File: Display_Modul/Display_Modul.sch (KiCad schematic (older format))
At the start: 14 parts, among them J101 Conn_01x08_Male, J102 Conn_02x08_Counter_Clockwise, SW101 Rotary_Encoder_Switch

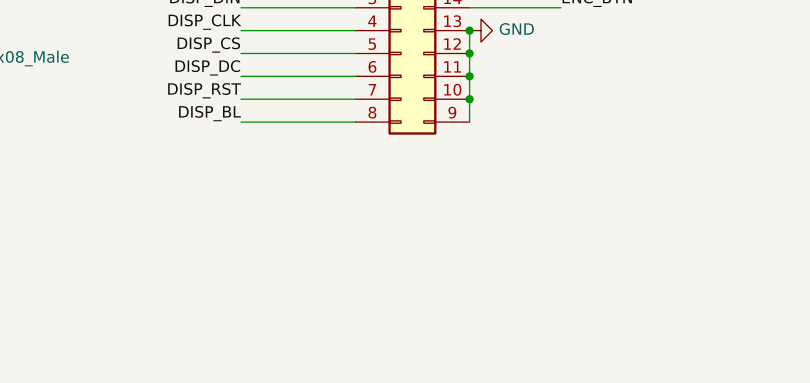
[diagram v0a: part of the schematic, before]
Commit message: Feeder Rails hinzugefügt
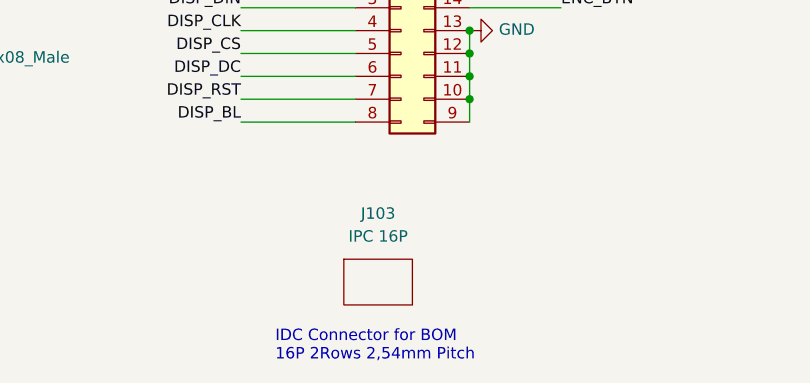
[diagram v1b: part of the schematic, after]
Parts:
- added J103: IPC 16P, ProjectFootprints:Empty, symbol PorjectLibrary:Empty
- H101, H102, H103, H104, J101: LCSC (none) -> 0
- J102: LCSC (none) -> C3406
- SW101: LCSC (none) -> C1322538
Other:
- note added: "IDC Connector for BOM\n16P 2Rows 2,54mm Pitch"
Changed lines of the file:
@@
 F 2 "Rotary_Encoder:RotaryEncoder_Alps_EC11E-Switch_Vertical_H20mm_CircularMountingHoles" H 5300 3310 50  0001 C CNN
 F 3 "~" H 5450 3410 50  0001 C CNN
+F 4 "C1322538" H 5450 3150 50  0001 C CNN "LCSC"
 	1    5450 3150
 	1    0    0    -1
@@
 F 2 "ProjectFootprints:ST7789_Waveshare" H 3850 4650 50  0001 C CNN
 F 3 "~" H 3850 4650 50  0001 C CNN
+F 4 "0" H 3850 4650 50  0001 C CNN "LCSC"
 	1    3850 4650
 	-1   0    0    -1
@@
 F 2 "ProjectFootprints:DisplayConnector" H 5950 4650 50  0001 C CNN
 F 3 "~" H 5950 4650 50  0001 C CNN
+F 4 "C3406" H 5950 4650 50  0001 C CNN "LCSC"
 	1    5950 4650
 	1    0    0    -1
@@
 F 2 "MountingHole:MountingHole_3.2mm_M3_Pad_Via" H 8000 3000 50  0001 C CNN
 F 3 "~" H 8000 3000 50  0001 C CNN
+F 4 "0" H 8000 3000 50  0001 C CNN "LCSC"
 	1    8000 3000
 	0    1    1    0
@@
 F 2 "MountingHole:MountingHole_3.2mm_M3_Pad_Via" H 8000 3200 50  0001 C CNN
 F 3 "~" H 8000 3200 50  0001 C CNN
+F 4 "0" H 8000 3200 50  0001 C CNN "LCSC"
 	1    8000 3200
 	0    1    1    0
@@
 F 2 "MountingHole:MountingHole_3.2mm_M3_Pad_Via" H 8000 3400 50  0001 C CNN
 F 3 "~" H 8000 3400 50  0001 C CNN
+F 4 "0" H 8000 3400 50  0001 C CNN "LCSC"
 	1    8000 3400
 	0    1    1    0
@@
 F 2 "MountingHole:MountingHole_3.2mm_M3_Pad_Via" H 8000 3600 50  0001 C CNN
 F 3 "~" H 8000 3600 50  0001 C CNN
+F 4 "0" H 8000 3600 50  0001 C CNN "LCSC"
 	1    8000 3600
 	0    1    1    0
@@
 Wire Wire Line
 	7900 3600 7900 4000
+$Comp
+L PorjectLibrary:Empty J103
+U 1 1 601D8426
+P 5850 5750
+F 0 "J103" H 5850 6050 50  0000 C CNN
+F 1 "IPC 16P" H 5850 5950 50  0000 C CNN
+F 2 "ProjectFootprints:Empty" H 5850 5750 50  0001 C CNN
+F 3 "~" H 5850 5750 50  0001 C CNN
+F 4 "C8372" H 5850 5750 50  0001 C CNN "LCSC"
+	1    5850 5750
+	1    0    0    -1
+$EndComp
+Text Notes 5400 6100 0    50   ~ 0
+IDC Connector for BOM\n16P 2Rows 2,54mm Pitch
 $EndSCHEMATC
